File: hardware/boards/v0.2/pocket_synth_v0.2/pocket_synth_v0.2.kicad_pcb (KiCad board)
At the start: 6 copper layers, 52 x 155 mm, 19 parts, among them SW1 SW_Push, SW2 SW_Push, SW3 SW_Push, SW4 SW_Push, U1 STM32H750XBHx, U2 STM32F401VEHx, U3 AS4C32M16SB-7BIN

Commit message: start rev2 schematic and layout
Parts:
- removed REF** (x2): Jack_3.5mm_CUI_SJ-3523-SMT_Horizontal, Connector_Audio:Jack_3.5mm_CUI_SJ-3523-SMT_Horizontal
- removed REF**: SD_Kyocera_145638009511859+, Connector_Card:SD_Kyocera_145638009511859+
- removed REF** (x2): Hirose_DF40C-90DS-0.4V_2x45_P0.4mm, Connector_Hirose_DF40:Hirose_DF40C-90DS-0.4V_2x45_P0.4mm
- removed REF** (x4): MountingHole_2.2mm_M2_Pad, MountingHole:MountingHole_2.2mm_M2_Pad
- removed REF**: QFN-32-1EP_4x4mm_P0.4mm_EP2.9x2.9mm, Package_DFN_QFN:QFN-32-1EP_4x4mm_P0.4mm_EP2.9x2.9mm
- removed REF**: USB_C_Receptacle_HCTL_HC-TYPE-C-16P-01A, Connector_USB:USB_C_Receptacle_HCTL_HC-TYPE-C-16P-01A
- added BT1: Battery, Connector_PinHeader_2.54mm:PinHeader_1x02_P2.54mm_Vertical, F.Cu at (80.9, 69.9)
- added C1: 100nf, Capacitor_SMD:C_0402_1005Metric, F.Cu at (66.8, 39.2)
- added C10: 100nf, Capacitor_SMD:C_0402_1005Metric, F.Cu at (67.4, 43.3)
- added C11: 100nf, Capacitor_SMD:C_0402_1005Metric, F.Cu at (66.0, 42.8)
- added C12: 100nf, Capacitor_SMD:C_0402_1005Metric, F.Cu at (67.4, 42.4)
- added C13: 100nf, Capacitor_SMD:C_0402_1005Metric, F.Cu at (62.1, 40.7)
- added C14: 100nf, Capacitor_SMD:C_0402_1005Metric, F.Cu at (63.0, 38.4)
- added C15: 100nf, Capacitor_SMD:C_0402_1005Metric, F.Cu at (61.6, 38.9)
- added C16: 100nf, Capacitor_SMD:C_0402_1005Metric, F.Cu at (63.2, 43.2)
- added C17: 100nf, Capacitor_SMD:C_0402_1005Metric, F.Cu at (65.1, 42.8)
- added C18: 100nf, Capacitor_SMD:C_0402_1005Metric, F.Cu at (62.1, 41.7)
- added C19: 100nf, Capacitor_SMD:C_0402_1005Metric, F.Cu at (62.1, 39.8)
- added C2: 100nf, Capacitor_SMD:C_0402_1005Metric, F.Cu at (66.8, 40.1)
- added C20: 100nf, Capacitor_SMD:C_0402_1005Metric, F.Cu at (64.3, 38.4)
- added C21: C, Capacitor_SMD:C_0805_2012Metric, F.Cu at (76.7, 42.6)
- added C22: C, Capacitor_SMD:C_0805_2012Metric, F.Cu at (74.5, 39.8)
- added C3: 100nf, Capacitor_SMD:C_0402_1005Metric, F.Cu at (61.9, 42.7)
- added C4: 4.7uF, Capacitor_SMD:C_0402_1005Metric, B.Cu at (94.4, 32.3)
- added C5: C, Capacitor_SMD:C_0805_2012Metric, F.Cu at (74.7, 33.7)
- added C6: 100nf, Capacitor_SMD:C_0402_1005Metric, F.Cu at (66.8, 38.3)
- added C7: C, Capacitor_SMD:C_0805_2012Metric, F.Cu at (76.8, 36.6)
- added C8: 100nf, Capacitor_SMD:C_0402_1005Metric, F.Cu at (66.9, 41.4)
- added C9: 100nf, Capacitor_SMD:C_0402_1005Metric, F.Cu at (58.5, 44.4)
- added J1: Conn_ARM_JTAG_SWD_10, Connector_PinHeader_1.27mm:PinHeader_2x05_P1.27mm_Vertical_SMD, B.Cu at (63.4, 21.4)
- added J2: DEVICE, Connector_USB:USB_C_Receptacle_HCTL_HC-TYPE-C-16P-01A, B.Cu at (46.1, 14.4)
- added J3: AudioJack3, Connector_Audio:Jack_3.5mm_CUI_SJ-3523-SMT_Horizontal, F.Cu at (-37.0, -6.80)
- added J4: AudioJack3, Connector_Audio:Jack_3.5mm_CUI_SJ-3523-SMT_Horizontal, F.Cu at (-24.8, -6.80)
- added J5: AudioJack3, Connector_Audio:Jack_3.5mm_CUI_SJ-3523-SMT_Horizontal, B.Cu at (19.0, 18.1)
- added J6: AudioJack3, Connector_Audio:Jack_3.5mm_CUI_SJ-3523-SMT_Horizontal, B.Cu at (23.0, 169.5)
- added J7: DISPLAY, Connector_FFC-FPC:Amphenol_F32Q-1A7x1-11053_1x53-1MP_P0.5mm_Horizontal, F.Cu at (41.3, 27.8)
- added J8: Micro_SD_Card_Det2, Connector_Card:microSD_HC_Hirose_DM3AT-SF-PEJM5, B.Cu at (81.1, 20.9)
- added J9: HOST, Connector_USB:USB_C_Receptacle_HCTL_HC-TYPE-C-16P-01A, F.Cu at (56.8, 14.4)
- added U4: STM32H753VIHx, Package_BGA:TFBGA-100_8x8mm_Layout10x10_P0.8mm, F.Cu at (-31.1, 48.5)
- added U5: W25Q128JVS, Package_SO:SOIC-8_5.3x5.3mm_P1.27mm, F.Cu at (-1.59, 36.1)
- added U6: SDRAM1, Package_BGA:Alliance_TFBGA-54_8x8mm_Layout9x9_P0.8mm, B.Cu at (81.4, 60.3)
- added Y1: 32.768kHz, Crystal:Crystal_SMD_Abracon_ABM10-4Pin_2.5x2.0mm, F.Cu at (74.3, 36.5)
- added Y2: HSE, Crystal:Crystal_SMD_Abracon_ABM10-4Pin_2.5x2.0mm, F.Cu at (74.1, 42.5)
- U1: value STM32H750XBHx -> STM32H743XIHx; moved to B.Cu
- U2: moved to F.Cu
- U3: value AS4C32M16SB-7BIN -> SDRAM0; footprint Package_BGA:FBGA-96_8x13mm_Layout9x16_P0.8mm -> Package_BGA:Alliance_TFBGA-54_8x8mm_Layout9x9_P0.8mm; moved to B.Cu
- moved U2 93.3 mm to (-2.50, 15.2), turned to 0 degrees
- moved MK2 68.0 mm to (-4.50, 22.8), turned to 0 degrees
- moved SW2 37.9 mm to (46.9, 90.7)
- moved U3 36.4 mm to (81.4, 50.3), turned to -90 degrees
- moved SW3 30.9 mm to (53.9, 100.2)
- moved SW1 27.5 mm to (54.1, 83.3)
- moved U1 24.7 mm to (64.4, 40.8), turned to 180 degrees
- moved SW4 17.5 mm to (61.0, 91.0)
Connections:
- U1 pad A1: Net-(U1-VSS-PadA1) -> GND
- U1 pad A13: unconnected-(U1-PC10-PadA13) -> /SDMMC1_D2
- U1 pad A17: Net-(U1-VSS-PadA1) -> GND
- U1 pad A8: unconnected-(U1-PK5-PadA8) -> /LCD_B6
- U1 pad B10: unconnected-(U1-PJ15-PadB10) -> /LCD_B3
- U1 pad B12: unconnected-(U1-PD3-PadB12) -> /FMC_CLK
- U1 pad B13: unconnected-(U1-PC11-PadB13) -> /SDMMC1_D3
- U1 pad B14: unconnected-(U1-PA14-PadB14) -> /SWD_CLK
- U1 pad B2: Net-(U1-VSS-PadA1) -> GND
- U1 pad B4: unconnected-(U1-PE1-PadB4) -> /FMC_NBL1
- U1 pad B6: Net-(U1-VSS-PadA1) -> GND
- U1 pad B8: unconnected-(U1-PK4-PadB8) -> /LCD_B5
- U1 pad C1: unconnected-(U1-PC15-PadC1) -> Net-(U1-PC15)
- U1 pad C10: Net-(U1-VSS-PadA1) -> GND
- U1 pad C11: unconnected-(U1-PD7-PadC11) -> /FMC_NE1
- U1 pad C12: unconnected-(U1-PC12-PadC12) -> /SDMMC1_CK
- U1 pad C13: Net-(U1-VSS-PadA1) -> GND
- U1 pad C15: unconnected-(U1-PA13-PadC15) -> /SWD_IO
- U1 pad C16: Net-(U1-VSS-PadA1) -> GND
- U1 pad C2: unconnected-(U1-PC14-PadC2) -> Net-(U1-PC14)
- U1 pad C4: unconnected-(U1-PE0-PadC4) -> /FMC_NBL0
- U1 pad C6: unconnected-(U1-PB3-PadC6) -> /SWD_SWO
- U1 pad C7: unconnected-(U1-PK6-PadC7) -> /LCD_B7
- U1 pad C8: unconnected-(U1-PK3-PadC8) -> /LCD_B4
- U1 pad D10: unconnected-(U1-PJ14-PadD10) -> /LCD_B2
- U1 pad D11: unconnected-(U1-PJ12-PadD11) -> /LCD_B0
- U1 pad D12: unconnected-(U1-PD2-PadD12) -> /SDMMC1_CMD
- U1 pad D13: unconnected-(U1-PD0-PadD13) -> /FMC_D2
- U1 pad D6: unconnected-(U1-PG15-PadD6) -> /FMC_SDNCAS
- U1 pad D7: unconnected-(U1-PK7-PadD7) -> /LCD_DE
- U1 pad E10: unconnected-(U1-PJ13-PadE10) -> /LCD_B1
- U1 pad E11: unconnected-(U1-VDD-PadE11) -> +3.3V
- U1 pad E12: unconnected-(U1-PD1-PadE12) -> /FMC_D3
- U1 pad E13: unconnected-(U1-PC8-PadE13) -> /SDMMC1_D0
- U1 pad E14: unconnected-(U1-PC9-PadE14) -> /SDMMC1_D1
- U1 pad E16: unconnected-(U1-PA12-PadE16) -> /USB_FS_D+
- U1 pad E17: unconnected-(U1-PA11-PadE17) -> /USB_FS_D-
- U1 pad E6: unconnected-(U1-VDD-PadE6) -> +3.3V
- U1 pad E9: unconnected-(U1-VDD-PadE9) -> +3.3V
- U1 pad F1: Net-(U1-VSS-PadA1) -> GND
- U1 pad F2: Net-(U1-VSS-PadA1) -> GND
- U1 pad F5: unconnected-(U1-VDD-PadF5) -> +3.3V
- U1 pad G1: unconnected-(U1-PF2-PadG1) -> /FMC_A2
- U1 pad G10: Net-(U1-VSS-PadA1) -> GND
- U1 pad G11: Net-(U1-VSS-PadA1) -> GND
- U1 pad G13: unconnected-(U1-VDD-PadG13) -> +3.3V
- U1 pad G14: unconnected-(U1-PG5-PadG14) -> /FMC_BA1
- U1 pad G15: unconnected-(U1-PG6-PadG15) -> /QSPI1_CS
- U1 pad G16: Net-(U1-VSS-PadA1) -> GND
- U1 pad G2: Net-(U1-VSS-PadA1) -> GND
- U1 pad G3: unconnected-(U1-PF1-PadG3) -> /FMC_A1
- U1 pad G4: unconnected-(U1-PF0-PadG4) -> /FMC_A0
- U1 pad G5: unconnected-(U1-VDD-PadG5) -> +3.3V
- U1 pad G7: Net-(U1-VSS-PadA1) -> GND
- U1 pad G8: Net-(U1-VSS-PadA1) -> GND
- U1 pad G9: Net-(U1-VSS-PadA1) -> GND
- U1 pad H10: Net-(U1-VSS-PadA1) -> GND
- U1 pad H11: Net-(U1-VSS-PadA1) -> GND
- U1 pad H13: unconnected-(U1-VDD-PadH13) -> +3.3V
- U1 pad H14: unconnected-(U1-PG4-PadH14) -> /FMC_BA0
- U1 pad H16: unconnected-(U1-PG2-PadH16) -> /FMC_A12
- U1 pad H17: unconnected-(U1-PK2-PadH17) -> /LCD_G7
- U1 pad H3: unconnected-(U1-PI14-PadH3) -> /LCD_CLK
- U1 pad H4: unconnected-(U1-PF3-PadH4) -> /FMC_A3
- U1 pad H5: unconnected-(U1-VDD-PadH5) -> +3.3V
- U1 pad H7: Net-(U1-VSS-PadA1) -> GND
- U1 pad H8: Net-(U1-VSS-PadA1) -> GND
- U1 pad H9: Net-(U1-VSS-PadA1) -> GND
- U1 pad J1: unconnected-(U1-PH1-PadJ1) -> Net-(U1-PH1)
- U1 pad J10: Net-(U1-VSS-PadA1) -> GND
- U1 pad J11: Net-(U1-VSS-PadA1) -> GND
- U1 pad J13: unconnected-(U1-VDD-PadJ13) -> +3.3V
- U1 pad J14: unconnected-(U1-PK0-PadJ14) -> /LCD_G5
- U1 pad J15: unconnected-(U1-PK1-PadJ15) -> /LCD_G6
- U1 pad J16: Net-(U1-VSS-PadA1) -> GND
- U1 pad J17: Net-(U1-VSS-PadA1) -> GND
- U1 pad J2: unconnected-(U1-PH0-PadJ2) -> Net-(U1-PH0)
- U1 pad J3: Net-(U1-VSS-PadA1) -> GND
- U1 pad J4: unconnected-(U1-PF5-PadJ4) -> /FMC_A5
- U1 pad J5: unconnected-(U1-PF4-PadJ5) -> /FMC_A4
- U1 pad J7: Net-(U1-VSS-PadA1) -> GND
- U1 pad J8: Net-(U1-VSS-PadA1) -> GND
- U1 pad J9: Net-(U1-VSS-PadA1) -> GND
- U1 pad K1: unconnected-(U1-NRST-PadK1) -> /SWD_RESET
- U1 pad K10: Net-(U1-VSS-PadA1) -> GND
- U1 pad K11: Net-(U1-VSS-PadA1) -> GND
- U1 pad K13: unconnected-(U1-VDD-PadK13) -> +3.3V
- U1 pad K14: unconnected-(U1-PJ11-PadK14) -> /LCD_G4
- U1 pad K15: Net-(U1-VSS-PadA1) -> GND
- U1 pad K2: unconnected-(U1-PF6-PadK2) -> /QSPI1_IO3
- U1 pad K3: unconnected-(U1-PF7-PadK3) -> /QSPI1_IO2
- U1 pad K4: unconnected-(U1-PF8-PadK4) -> /QSPI1_IO0
- U1 pad K5: unconnected-(U1-VDD-PadK5) -> +3.3V
- U1 pad K7: Net-(U1-VSS-PadA1) -> GND
- U1 pad K8: Net-(U1-VSS-PadA1) -> GND
- U1 pad K9: Net-(U1-VSS-PadA1) -> GND
- U1 pad L10: Net-(U1-VSS-PadA1) -> GND
- U1 pad L11: Net-(U1-VSS-PadA1) -> GND
- U1 pad L13: unconnected-(U1-VDD-PadL13) -> +3.3V
- U1 pad L14: unconnected-(U1-PJ10-PadL14) -> /LCD_G3
- U1 pad L15: Net-(U1-VSS-PadA1) -> GND
- U1 pad L3: unconnected-(U1-PF10-PadL3) -> /QSPI1_CLK
- U1 pad L4: unconnected-(U1-PF9-PadL4) -> /QSPI1_IO1
- U1 pad L5: unconnected-(U1-VDD-PadL5) -> +3.3V
- U1 pad L7: Net-(U1-VSS-PadA1) -> GND
- U1 pad L8: Net-(U1-VSS-PadA1) -> GND
- U1 pad L9: Net-(U1-VSS-PadA1) -> GND
- U1 pad M13: unconnected-(U1-VDD-PadM13) -> +3.3V
- U1 pad M14: unconnected-(U1-PJ9-PadM14) -> /LCD_G2
- U1 pad M15: Net-(U1-VSS-PadA1) -> GND
- U1 pad M5: unconnected-(U1-VDD-PadM5) -> +3.3V
- U1 pad N10: unconnected-(U1-VDD-PadN10) -> +3.3V
- U1 pad N11: unconnected-(U1-VDD-PadN11) -> +3.3V
- U1 pad N12: unconnected-(U1-VDD-PadN12) -> +3.3V
- U1 pad N13: unconnected-(U1-PJ8-PadN13) -> /LCD_G1
- U1 pad N14: unconnected-(U1-PJ7-PadN14) -> /LCD_G0
- U1 pad N15: unconnected-(U1-PJ6-PadN15) -> /LCD_R7
- U1 pad N16: Net-(U1-VSS-PadA1) -> GND
- U1 pad N6: unconnected-(U1-PJ0-PadN6) -> /LCD_R1
- U1 pad N7: unconnected-(U1-VDD-PadN7) -> +3.3V
- U1 pad N8: unconnected-(U1-VDD-PadN8) -> +3.3V
- U1 pad N9: unconnected-(U1-PE10-PadN9) -> /FMC_D7
- U1 pad P1: unconnected-(U1-VSSA-PadP1) -> GND
- U1 pad P10: unconnected-(U1-PE11-PadP10) -> /FMC_D8
- U1 pad P15: unconnected-(U1-PD15-PadP15) -> /FMC_D1
- U1 pad P16: unconnected-(U1-PD14-PadP16) -> /FMC_D0
- U1 pad P17: unconnected-(U1-VDD-PadP17) -> +3.3V
- U1 pad P2: unconnected-(U1-PH3-PadP2) -> /FMC_SDNE0
- U1 pad P4: unconnected-(U1-PH5-PadP4) -> /FMC_SDNWE
- U1 pad P5: unconnected-(U1-PI15-PadP5) -> /LCD_R0
- U1 pad P6: unconnected-(U1-PJ1-PadP6) -> /LCD_R2
- U1 pad P7: unconnected-(U1-PF13-PadP7) -> /FMC_A7
- U1 pad P8: unconnected-(U1-PF14-PadP8) -> /FMC_A8
- U1 pad P9: unconnected-(U1-PE9-PadP9) -> /FMC_D6
- U1 pad R10: unconnected-(U1-PE12-PadR10) -> /FMC_D9
- U1 pad R11: unconnected-(U1-PE15-PadR11) -> /FMC_D12
- U1 pad R12: unconnected-(U1-PJ5-PadR12) -> /LCD_R6
- U1 pad R4: Net-(U1-VSS-PadA1) -> GND
- U1 pad R7: unconnected-(U1-PF12-PadR7) -> /FMC_A6
- U1 pad R8: Net-(U1-VSS-PadA1) -> GND
- U1 pad R9: unconnected-(U1-PF15-PadR9) -> /FMC_A8
- U1 pad T10: unconnected-(U1-PE13-PadT10) -> /FMC_D10
- U1 pad T12: Net-(U1-VSS-PadA1) -> GND
- U1 pad T15: unconnected-(U1-PB15-PadT15) -> /USB_HS_D+
- U1 pad T16: unconnected-(U1-PD10-PadT16) -> /FMC_D15
- U1 pad T17: unconnected-(U1-PD9-PadT17) -> /FMC_D14
- U1 pad T6: unconnected-(U1-PJ2-PadT6) -> /LCD_R3
- U1 pad T7: unconnected-(U1-PF11-PadT7) -> /FMC_SDNRAS
- U1 pad T8: unconnected-(U1-PG0-PadT8) -> /FMC_A10
- U1 pad T9: unconnected-(U1-PE8-PadT9) -> /FMC_D5
- U1 pad U1: Net-(U1-VSS-PadA1) -> GND
- U1 pad U10: unconnected-(U1-PE14-PadU10) -> /FMC_D11
- U1 pad U13: unconnected-(U1-PH7-PadU13) -> /FMC_SDCKE1
- U1 pad U15: unconnected-(U1-PB14-PadU15) -> /USB_HS_D-
- U1 pad U16: unconnected-(U1-PD8-PadU16) -> /FMC_D13
- U1 pad U17: Net-(U1-VSS-PadA1) -> GND
- U1 pad U4: unconnected-(U1-PC5-PadU4) -> /FMC_SDCKE0
- U1 pad U6: unconnected-(U1-PJ3-PadU6) -> /LCD_R4
- U1 pad U7: unconnected-(U1-PJ4-PadU7) -> /LCD_R5
- U1 pad U8: unconnected-(U1-PG1-PadU8) -> /FMC_A11
- U1 pad U9: unconnected-(U1-PE7-PadU9) -> /FMC_D4
- U3 pad A1: VSS -> GND
- U3 pad A2: unconnected-(U3-DQ15-PadA2) -> /FMC_D15
- U3 pad A3: VSSQ -> GND
- U3 pad A7: VDDQ -> +3.3V
- U3 pad A8: unconnected-(U3-DQ0-PadA8) -> /FMC_D0
- U3 pad A9: VDD -> +3.3V
- U3 pad B1: unconnected-(U3-DQ14-PadB1) -> /FMC_D14
- U3 pad B2: unconnected-(U3-DQ13-PadB2) -> /FMC_D13
- U3 pad B3: VDDQ -> +3.3V
- U3 pad B7: VSSQ -> GND
- U3 pad B8: unconnected-(U3-DQ2-PadB8) -> /FMC_D2
- U3 pad B9: unconnected-(U3-DQ1-PadB9) -> /FMC_D1
- U3 pad C1: unconnected-(U3-DQ12-PadC1) -> /FMC_D12
- U3 pad C2: unconnected-(U3-DQ11-PadC2) -> /FMC_D11
- U3 pad C3: VSSQ -> GND
- U3 pad C7: VDDQ -> +3.3V
- U3 pad C8: unconnected-(U3-DQ4-PadC8) -> /FMC_D4
- U3 pad C9: unconnected-(U3-DQ3-PadC9) -> /FMC_D3
- U3 pad D1: unconnected-(U3-DQ10-PadD1) -> /FMC_D10
- U3 pad D2: unconnected-(U3-DQ9-PadD2) -> /FMC_D9
- U3 pad D3: VDDQ -> +3.3V
- U3 pad D7: VSSQ -> GND
- U3 pad D8: unconnected-(U3-DQ6-PadD8) -> /FMC_D6
- U3 pad D9: unconnected-(U3-DQ5-PadD9) -> /FMC_D5
- U3 pad E1: unconnected-(U3-DQ8-PadE1) -> /FMC_D8
- U3 pad E3: VSS -> GND
- U3 pad E7: VDD -> +3.3V
- U3 pad E8: unconnected-(U3-LDQM-PadE8) -> /FMC_NBL0
- U3 pad E9: unconnected-(U3-DQ7-PadE9) -> /FMC_D7
- U3 pad F1: unconnected-(U3-UDQM-PadF1) -> /FMC_NBL1
- U3 pad F2: unconnected-(U3-CLK-PadF2) -> /FMC_CLK
- U3 pad F3: unconnected-(U3-CKE-PadF3) -> /FMC_SDCKE0
- U3 pad F7: unconnected-(U3-CAS#-PadF7) -> /FMC_SDNCAS
- U3 pad F8: unconnected-(U3-RAS#-PadF8) -> /FMC_SDNRAS
- U3 pad F9: unconnected-(U3-WE#-PadF9) -> /FMC_SDNWE
- U3 pad G1: unconnected-(U3-A12-PadG1) -> /FMC_A12
- U3 pad G2: unconnected-(U3-A11-PadG2) -> /FMC_A11
- U3 pad G3: unconnected-(U3-A9-PadG3) -> /FMC_A8
- U3 pad G7: unconnected-(U3-BA0-PadG7) -> /FMC_BA0
- U3 pad G8: unconnected-(U3-BA1-PadG8) -> /FMC_BA1
- U3 pad G9: unconnected-(U3-CS#-PadG9) -> /FMC_SDNE0
- U3 pad H1: unconnected-(U3-A8-PadH1) -> /FMC_A8
- U3 pad H2: unconnected-(U3-A7-PadH2) -> /FMC_A7
- U3 pad H3: unconnected-(U3-A6-PadH3) -> /FMC_A6
- U3 pad H7: unconnected-(U3-A0-PadH7) -> /FMC_A0
- U3 pad H8: unconnected-(U3-A1-PadH8) -> /FMC_A1
- U3 pad H9: unconnected-(U3-A10-PadH9) -> /FMC_A10
- U3 pad J1: VSS -> GND
- U3 pad J2: unconnected-(U3-A5-PadJ2) -> /FMC_A5
- U3 pad J3: unconnected-(U3-A4-PadJ3) -> /FMC_A4
- U3 pad J7: unconnected-(U3-A3-PadJ7) -> /FMC_A3
- U3 pad J8: unconnected-(U3-A2-PadJ8) -> /FMC_A2
- U3 pad J9: VDD -> +3.3V
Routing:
- net GND: track 0.00 -> 17.2 mm, vias 0 -> 60
- net /FMC_A8: track 0.00 -> 7.27 mm, vias 0 -> 2
- net /SDMMC1_D0: track 0.00 -> 5.00 mm, vias 0 -> 1
- net /LCD_B1: track 0.00 -> 4.99 mm, vias 0 -> 1
- net /FMC_D3: track 0.00 -> 4.97 mm, vias 0 -> 1
- net /FMC_A4: track 0.00 -> 4.96 mm, vias 0 -> 1
- net /LCD_R1: track 0.00 -> 4.93 mm, vias 0 -> 1
- net /FMC_D7: track 0.00 -> 4.93 mm, vias 0 -> 1
- net /LCD_G1: track 0.00 -> 4.91 mm, vias 0 -> 1
- net +3.3V: track 0.00 -> 4.24 mm, vias 0 -> 34
- net /LCD_DE: track 0.00 -> 4.20 mm, vias 0 -> 1
- net /QSPI1_IO0: track 0.00 -> 4.19 mm, vias 0 -> 1
- net /LCD_G5: track 0.00 -> 4.19 mm, vias 0 -> 1
- net /LCD_B0: track 0.00 -> 4.18 mm, vias 0 -> 1
- net /FMC_A5: track 0.00 -> 4.17 mm, vias 0 -> 1
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- added copper zone on In2.Cu, net +3.3V
- added copper zone on B.Cu, net GND
- added copper zone on F.Cu, net GND
- added copper zone on In1.Cu, net GND
- added copper zone on In4.Cu, net GND
- added copper zone on In6.Cu, net GND
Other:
- board size 52 x 155 mm -> 77 x 164 mm
- copper layers 6 -> 8
- board text added: "Back FPC Entry"
- board text added: "Display FPC"
- board text added: "FPC Component Area"
- board text added: "Touch FPC"

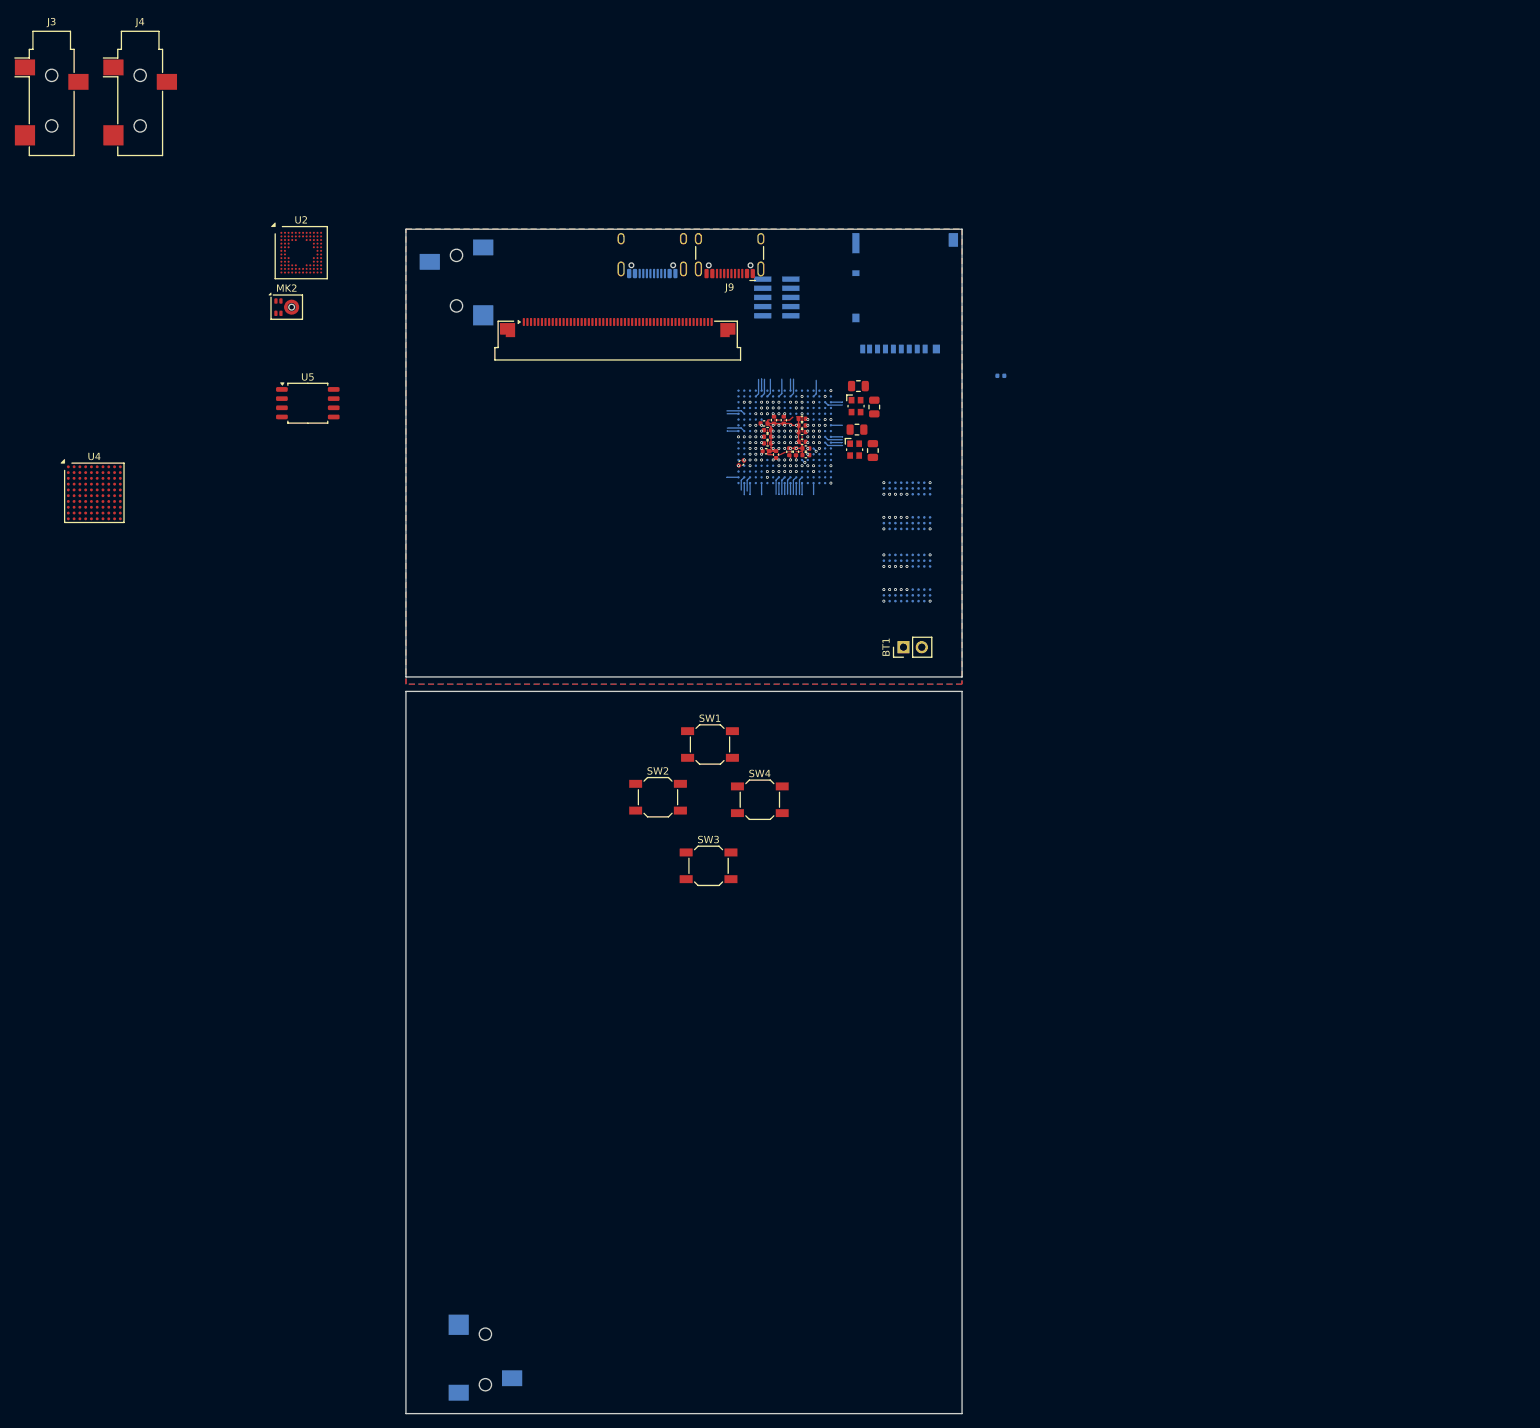
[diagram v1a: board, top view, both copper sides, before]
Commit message: start SDRAM routing
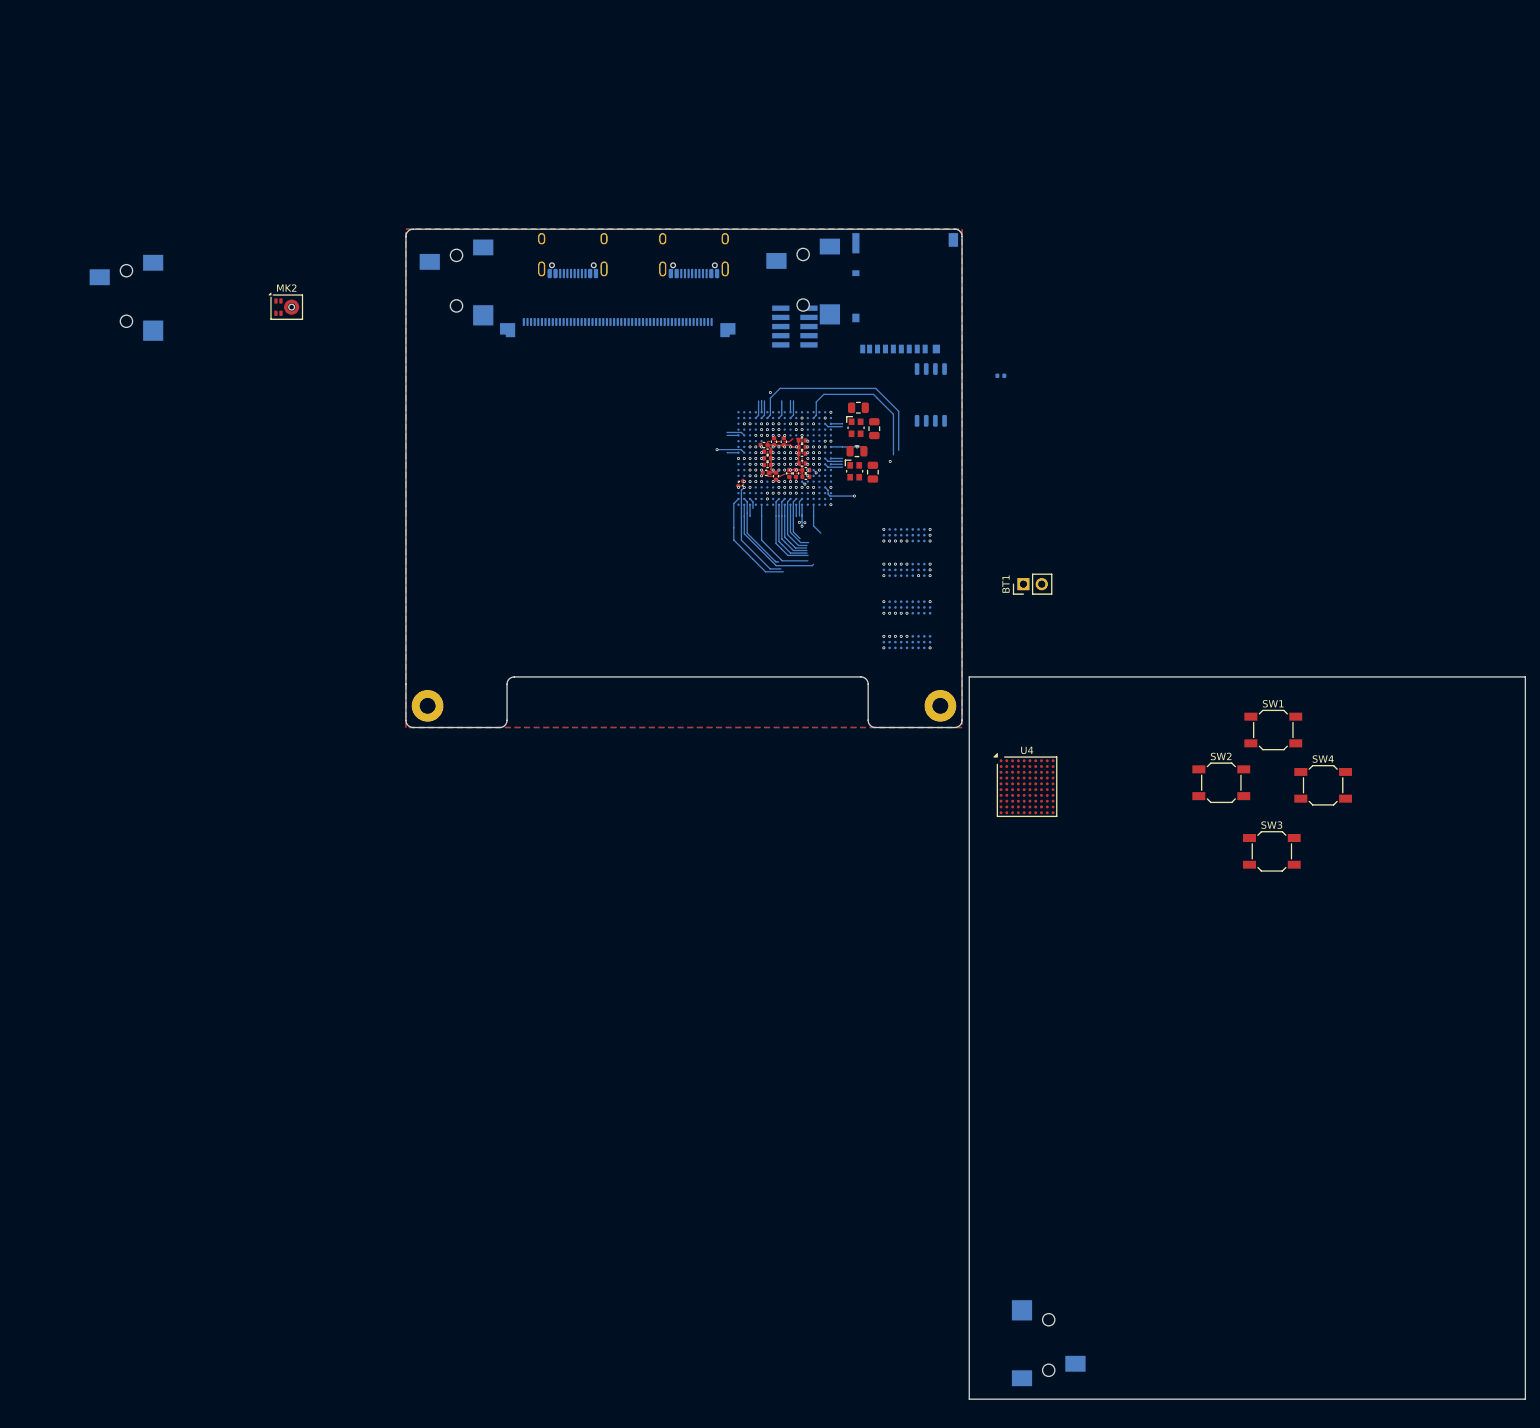
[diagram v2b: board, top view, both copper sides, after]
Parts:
- removed U2: STM32F401VEHx, Package_BGA:UFBGA-100_7x7mm_Layout12x12_P0.5mm
- added H1: MountingHole_Pad, MountingHole:MountingHole_2.2mm_M2_Pad, F.Cu at (15.0, 78.0)
- added H2: MountingHole_Pad, MountingHole:MountingHole_2.2mm_M2_Pad, F.Cu at (86.0, 78.0)
- J3, J4, J7, J9, U5: moved to B.Cu
- moved U4 135.4 mm to (98.0, 89.2)
- moved J3 107.0 mm to (67.0, 18.0), turned to 180 degrees
- moved U5 86.3 mm to (84.7, 35.0), turned to -90 degrees
- moved J6 78.0 mm to (101.0, 167.5)
- moved SW1 78.0 mm to (132.1, 81.3)
- moved SW2 78.0 mm to (124.9, 88.7)
- moved SW3 78.0 mm to (131.9, 98.2)
- moved SW4 78.0 mm to (139.0, 89.0)
- moved J4 27.1 mm to (-26.7, 20.2), turned to 180 degrees
- moved BT1 18.8 mm to (97.5, 61.1)
- moved J2 11.0 mm to (35.1, 14.4)
- moved U6 6.48 mm to (81.4, 66.8)
- moved U3 6.48 mm to (81.4, 56.8)
- moved J9 4.94 mm to (51.9, 14.4), turned to 0 degrees
- moved J1 4.74 mm to (65.8, 25.5)
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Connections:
- U1 pad R9: /FMC_A8 -> /FMC_A9
- U3 pad G3: /FMC_A8 -> /FMC_A9
- U6 pad G3: /FMC_A8 -> /FMC_A9
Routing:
- net /FMC_BA1: track 4.14 -> 36.8 mm
- net /FMC_A2: track 1.58 -> 30.8 mm, vias 0 -> 2
- net /FMC_BA0: track 3.92 -> 33.1 mm
- net /FMC_A12: track 2.52 -> 29.6 mm, vias 0 -> 1
- net /FMC_D2: track 4.17 -> 30.6 mm
- net /FMC_A3: track 4.15 -> 29.7 mm, vias 1 -> 2
- net /FMC_CLK: track 2.56 -> 28.0 mm
- net /FMC_D3: track 4.97 -> 28.9 mm, vias 1 -> 2
- net /FMC_SDNE0: track 0.00 -> 23.3 mm, vias 0 -> 2
- net /FMC_D1: track 3.26 -> 25.9 mm
- net /FMC_NE1: track 3.22 -> 25.4 mm
- net /FMC_A4: track 4.96 -> 25.9 mm, vias 1 -> 3
- net /FMC_A5: track 4.17 -> 23.3 mm, vias 1 -> 2
- net /FMC_SDNCAS: track 4.15 -> 22.2 mm
- net /FMC_NBL1: track 2.38 -> 20.3 mm
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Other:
- board size 77 x 164 mm -> 155 x 162 mm
- board text removed: "Back FPC Entry"
- board text removed: "Touch FPC"

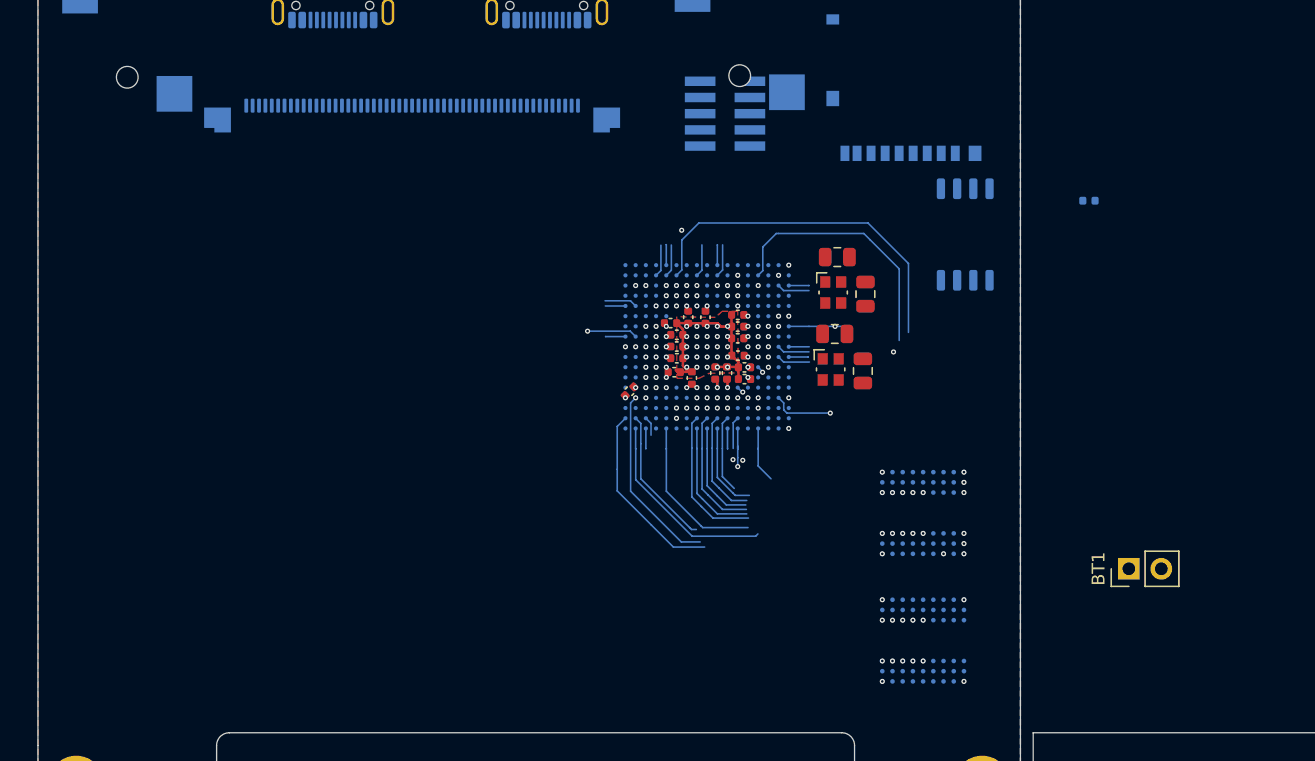
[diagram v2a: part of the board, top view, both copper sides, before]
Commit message: routed right side of SDRAM
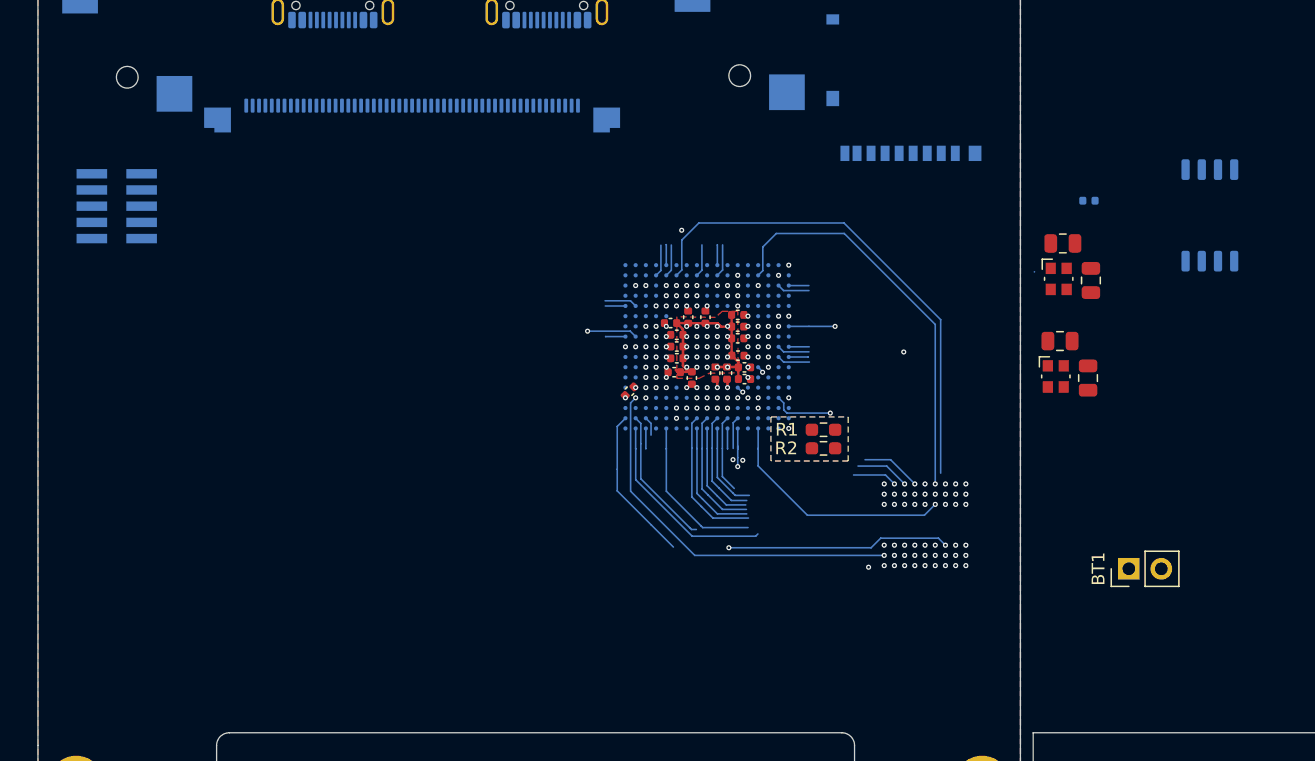
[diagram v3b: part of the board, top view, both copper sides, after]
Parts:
- removed U6: SDRAM1, Package_BGA:Alliance_TFBGA-54_8x8mm_Layout9x9_P0.8mm
- added R1: 10k, Resistor_SMD:R_0603_1608Metric_Pad0.98x0.95mm_HandSolder, F.Cu at (73.6, 50.2)
- added R2: 10k, Resistor_SMD:R_0603_1608Metric_Pad0.98x0.95mm_HandSolder, F.Cu at (73.6, 51.7)
- U3: value SDRAM0 -> SDRAM; footprint Package_BGA:Alliance_TFBGA-54_8x8mm_Layout9x9_P0.8mm -> S42S16320F-7BLI:IC54_IS42S16320F-7BLI_ISI
- moved J1 48.2 mm to (18.2, 32.7), turned to 0 degrees
- moved U5 19.2 mm to (103.8, 33.5)
- moved C7 17.7 mm to (94.5, 38.5)
- moved C5 17.7 mm to (92.3, 35.6)
- moved Y1 17.7 mm to (92.0, 38.4)
- moved Y2 17.7 mm to (91.8, 46.1)
- moved C21 17.7 mm to (94.3, 46.2)
- moved C22 17.7 mm to (92.1, 43.3)
- moved U3 0.94 mm to (81.5, 57.7)
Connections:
- U1 pad C11: /FMC_NE1 -> unconnected-(U1-PD7-PadC11)
- U1 pad U13: /FMC_SDCKE1 -> unconnected-(U1-PH7-PadU13)
- U1 pad U3: unconnected-(U1-PA4-PadU3) -> /MEM_SELECT
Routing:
- net /FMC_D2: track 30.6 -> 65.9 mm, vias 1 -> 2
- net /FMC_D3: track 28.9 -> 62.4 mm, vias 2 -> 3
- net /FMC_NBL0: track 19.7 -> 51.4 mm, vias 1 -> 2
- net /FMC_SDNCAS: track 22.2 -> 51.7 mm, vias 1 -> 2
- net /FMC_A1: track 8.04 -> 34.8 mm, vias 1 -> 2
- net /FMC_NE1: track 25.4 -> 0.00 mm, vias 1 -> 0
- net /FMC_A0: track 8.58 -> 33.1 mm, vias 1 -> 2
- net /FMC_BA0: track 33.1 -> 52.4 mm, vias 1 -> 3
- net /FMC_BA1: track 36.8 -> 55.7 mm, vias 1 -> 3
- net /FMC_SDNE0: track 23.3 -> 4.87 mm
- net /FMC_A9: track 9.41 -> 26.4 mm, vias 1 -> 2
- net /FMC_A6: track 7.40 -> 24.1 mm, vias 1 -> 2
- net /FMC_D0: track 14.6 -> 29.4 mm, vias 1 -> 2
- net /FMC_SDCKE0: track 4.38 -> 18.8 mm, vias 0 -> 1
- net /FMC_D1: track 25.9 -> 38.8 mm, vias 1 -> 2
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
